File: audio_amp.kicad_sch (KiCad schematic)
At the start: 9 parts, among them Q1201 BSS138, U1201 LM380N

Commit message: Update pcb database to version 6
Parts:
- C1201, C1206: symbol Custom:C_US_0805_0.1UF_X7R_10%_50V_HS -> custom:C_US_0805_0.1UF_X7R_10%_50V_HS
- C1202, C1205: symbol Custom:CP_US -> custom:CP_US; PartNumber 800270-477 -> 80000X-XXX
- C1203, C1204: symbol Custom:C_US -> custom:C_US; PartNumber 800003-475 -> 800063-XXX
- Q1201: symbol Custom:BSS138 -> custom:BSS138
- R1201: symbol Custom:R_US_0805_1%_HS -> custom:R_US_0805_1%_HS; PartNumber 800235-027 -> 800235-XXX
- U1201: symbol Custom:LM380N -> custom:LM380N
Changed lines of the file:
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@@
     (effects (font (size 1.27 1.27)) (justify right))
   )
-  (symbol (lib_id "Custom:C_US") (at 67.31 90.17 270) (unit 1)
+  (symbol (lib_id "custom:C_US") (at 67.31 90.17 270) (unit 1)
     (in_bom yes) (on_board yes)
     (property "Reference" "C1204" (id 0) (at 67.31 83.3882 90))
@@
       (effects (font (size 1.524 1.524)))
     )
-    (property "PartNumber" "800003-475" (id 4) (at 81.28 90.17 0)
-      (effects (font (size 1.524 1.524)) hide)
-    )
-    (pin "1")
-    (pin "2")
-  )
-  (symbol (lib_id "Custom:LM380N") (at 129.54 95.25 0) (unit 1)
+    (property "PartNumber" "800063-XXX" (id 4) (at 81.28 90.17 0)
+      (effects (font (size 1.524 1.524)) hide)
+    )
+    (pin "1")
+    (pin "2")
+  )
+  (symbol (lib_id "custom:LM380N") (at 129.54 95.25 0) (unit 1)
     (in_bom yes) (on_board yes)
     (property "Reference" "U1201" (id 0) (at 139.7 88.9 0)
@@
     (pin "9")
   )
-  (symbol (lib_id "Custom:GND_US") (at 121.92 123.19 0) (unit 1)
+  (symbol (lib_id "custom:GND_US") (at 121.92 123.19 0) (unit 1)
     (in_bom yes) (on_board yes)
     (property "Reference" "#PWR01203" (id 0) (at 121.412 126.492 0)
@@
     (pin "1")
   )
-  (symbol (lib_id "Custom:C_US") (at 146.05 78.74 90) (unit 1)
+  (symbol (lib_id "custom:C_US") (at 146.05 78.74 90) (unit 1)
     (in_bom yes) (on_board yes)
     (property "Reference" "C1203" (id 0) (at 146.05 85.5218 90))
@@
       (effects (font (size 1.524 1.524)))
     )
-    (property "PartNumber" "800003-475" (id 4) (at 132.08 78.74 0)
-      (effects (font (size 1.524 1.524)) hide)
-    )
-    (pin "1")
-    (pin "2")
-  )
-  (symbol (lib_id "Custom:GND_US") (at 157.48 85.09 0) (unit 1)
+    (property "PartNumber" "800063-XXX" (id 4) (at 132.08 78.74 0)
+      (effects (font (size 1.524 1.524)) hide)
+    )
+    (pin "1")
+    (pin "2")
+  )
+  (symbol (lib_id "custom:GND_US") (at 157.48 85.09 0) (unit 1)
     (in_bom yes) (on_board yes)
     (property "Reference" "#PWR01201" (id 0) (at 156.972 88.392 0)
@@
     (pin "1")
   )
-  (symbol (lib_id "Custom:R_US_0805_1%_HS") (at 151.13 104.14 0) (unit 1)
+  (symbol (lib_id "custom:R_US_0805_1%_HS") (at 151.13 104.14 0) (unit 1)
     (in_bom yes) (on_board yes)
     (property "Reference" "R1201" (id 0) (at 152.654 102.9716 0)
@@
       (effects (font (size 1.524 1.524)))
     )
-    (property "PartNumber" "800235-027" (id 4) (at 155.702 101.6 90)
-      (effects (font (size 1.524 1.524)) hide)
-    )
-    (pin "1")
-    (pin "2")
-  )
-  (symbol (lib_id "Custom:C_US_0805_0.1UF_X7R_10%_50V_HS") (at 151.13 118.11 0) (unit 1)
+    (property "PartNumber" "800235-XXX" (id 4) (at 155.702 101.6 90)
+      (effects (font (size 1.524 1.524)) hide)
+    )
+    (pin "1")
+    (pin "2")
+  )
+  (symbol (lib_id "custom:C_US_0805_0.1UF_X7R_10%_50V_HS") (at 151.13 118.11 0) (unit 1)
     (in_bom yes) (on_board yes)
     (property "Reference" "C1206" (id 0) (at 154.432 116.9416 0)
@@
     (pin "2")
   )
-  (symbol (lib_id "Custom:GND_US") (at 151.13 123.19 0) (unit 1)
+  (symbol (lib_id "custom:GND_US") (at 151.13 123.19 0) (unit 1)
     (in_bom yes) (on_board yes)
     (property "Reference" "#PWR01204" (id 0) (at 150.622 126.492 0)
@@
     (pin "1")
   )
-  (symbol (lib_id "Custom:CP_US") (at 170.18 95.25 90) (unit 1)
+  (symbol (lib_id "custom:CP_US") (at 170.18 95.25 90) (unit 1)
     (in_bom yes) (on_board yes)
     (property "Reference" "C1205" (id 0) (at 170.18 88.4682 90))
@@
       (effects (font (size 1.524 1.524)))
     )
-    (property "PartNumber" "800270-477" (id 4) (at 165.1 91.44 0)
-      (effects (font (size 1.524 1.524)) hide)
-    )
-    (pin "1")
-    (pin "2")
-  )
-  (symbol (lib_id "Custom:CP_US") (at 140.97 69.85 90) (unit 1)
+    (property "PartNumber" "80000X-XXX" (id 4) (at 165.1 91.44 0)
+      (effects (font (size 1.524 1.524)) hide)
+    )
+    (pin "1")
+    (pin "2")
+  )
+  (symbol (lib_id "custom:CP_US") (at 140.97 69.85 90) (unit 1)
     (in_bom yes) (on_board yes)
     (property "Reference" "C1202" (id 0) (at 140.97 63.0682 90))
@@
       (effects (font (size 1.524 1.524)))
     )
-    (property "PartNumber" "800270-477" (id 4) (at 135.89 66.04 0)
-      (effects (font (size 1.524 1.524)) hide)
-    )
-    (pin "1")
-    (pin "2")
-  )
-  (symbol (lib_id "Custom:C_US_0805_0.1UF_X7R_10%_50V_HS") (at 140.97 58.42 90) (unit 1)
+    (property "PartNumber" "80000X-XXX" (id 4) (at 135.89 66.04 0)
+      (effects (font (size 1.524 1.524)) hide)
+    )
+    (pin "1")
+    (pin "2")
+  )
+  (symbol (lib_id "custom:C_US_0805_0.1UF_X7R_10%_50V_HS") (at 140.97 58.42 90) (unit 1)
     (in_bom yes) (on_board yes)
     (property "Reference" "C1201" (id 0) (at 140.97 51.6382 90))
@@
     (pin "2")
   )
-  (symbol (lib_id "Custom:BSS138") (at 53.34 111.76 0) (unit 1)
+  (symbol (lib_id "custom:BSS138") (at 53.34 111.76 0) (unit 1)
     (in_bom yes) (on_board yes)
     (property "Reference" "Q1201" (id 0) (at 58.7756 110.7948 0)
@@
     (pin "3")
   )
-  (symbol (lib_id "Custom:GND_US") (at 55.88 121.92 0) (unit 1)
+  (symbol (lib_id "custom:GND_US") (at 55.88 121.92 0) (unit 1)
     (in_bom yes) (on_board yes)
     (property "Reference" "#PWR01202" (id 0) (at 55.372 125.222 0)

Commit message: Fix BOM part number errors and out of sync footprints which happened during conversion from Kicad 5 to 6
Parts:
- C1202, C1205: PartNumber 80000X-XXX -> 800277-477
- C1203, C1204: PartNumber 800063-XXX -> 800003-475
- R1201: PartNumber 800235-XXX -> 800235-027
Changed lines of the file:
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@@
       (effects (font (size 1.524 1.524)))
     )
-    (property "PartNumber" "800063-XXX" (id 4) (at 81.28 90.17 0)
+    (property "PartNumber" "800003-475" (id 4) (at 81.28 90.17 0)
       (effects (font (size 1.524 1.524)) hide)
     )
@@
       (effects (font (size 1.524 1.524)))
     )
-    (property "PartNumber" "800063-XXX" (id 4) (at 132.08 78.74 0)
+    (property "PartNumber" "800003-475" (id 4) (at 132.08 78.74 0)
       (effects (font (size 1.524 1.524)) hide)
     )
@@
       (effects (font (size 1.524 1.524)))
     )
-    (property "PartNumber" "800235-XXX" (id 4) (at 155.702 101.6 90)
+    (property "PartNumber" "800235-027" (id 4) (at 155.702 101.6 90)
       (effects (font (size 1.524 1.524)) hide)
     )
@@
       (effects (font (size 1.524 1.524)))
     )
-    (property "PartNumber" "80000X-XXX" (id 4) (at 165.1 91.44 0)
+    (property "PartNumber" "800277-477" (id 4) (at 165.1 91.44 0)
       (effects (font (size 1.524 1.524)) hide)
     )
@@
       (effects (font (size 1.524 1.524)))
     )
-    (property "PartNumber" "80000X-XXX" (id 4) (at 135.89 66.04 0)
+    (property "PartNumber" "800277-477" (id 4) (at 135.89 66.04 0)
       (effects (font (size 1.524 1.524)) hide)
     )

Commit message: Fix incorrect part number for 470uf capacitor
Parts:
- C1202, C1205: PartNumber 800277-477 -> 800270-477
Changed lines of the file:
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@@
       (effects (font (size 1.524 1.524)))
     )
-    (property "PartNumber" "800277-477" (id 4) (at 165.1 91.44 0)
+    (property "PartNumber" "800270-477" (id 4) (at 165.1 91.44 0)
       (effects (font (size 1.524 1.524)) hide)
     )
@@
       (effects (font (size 1.524 1.524)))
     )
-    (property "PartNumber" "800277-477" (id 4) (at 135.89 66.04 0)
+    (property "PartNumber" "800270-477" (id 4) (at 135.89 66.04 0)
       (effects (font (size 1.524 1.524)) hide)
     )

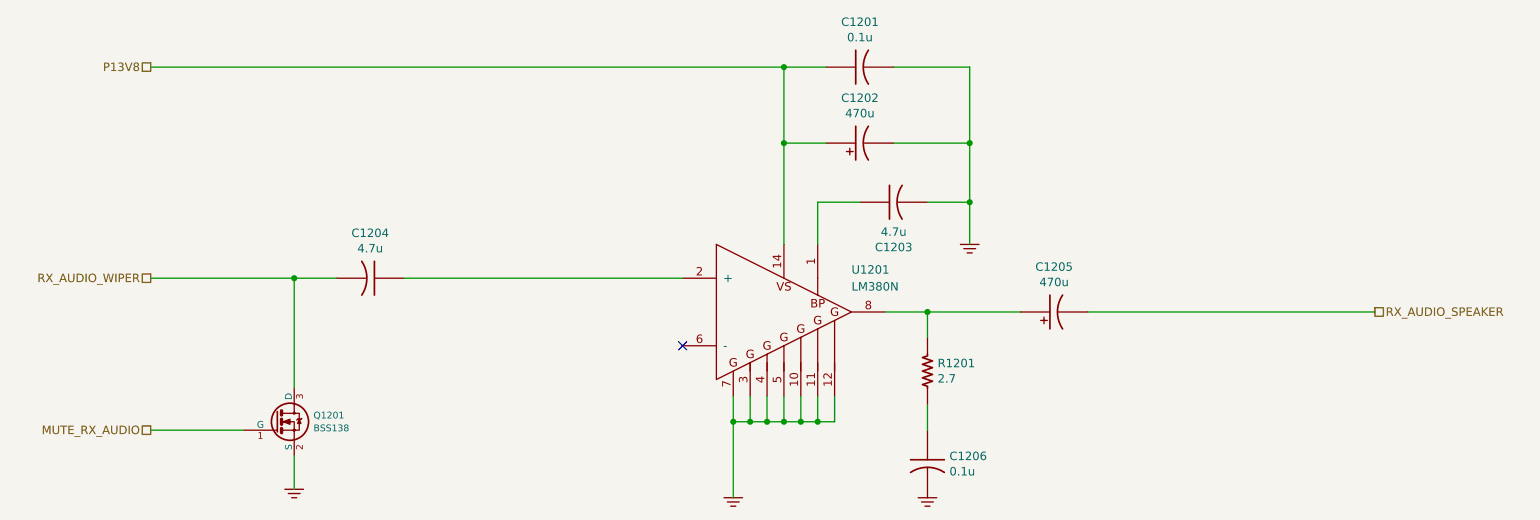
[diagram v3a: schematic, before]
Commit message: trx_mobo_concept_2_B. Change design to use a dedicated 8V supply for the 2SC3357 parts. Add S-Meter connector. Change mic connector to 3 pins and add 8V sopower supply to pin 3.
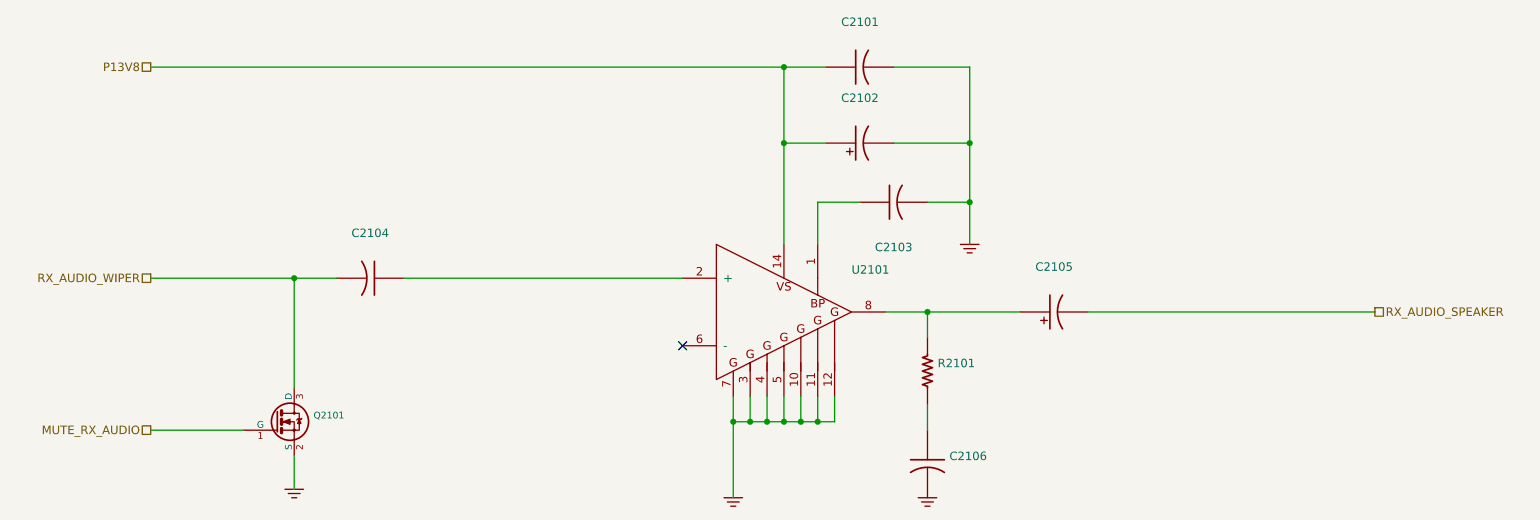
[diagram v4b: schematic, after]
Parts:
- C2101: renamed from C1201; value 0.1u -> (none); footprint Capacitor_SMD:C_0805_2012Metric_Pad1.15x1.40mm_HandSolder -> (none)
- C2102: renamed from C1202; value 470u -> (none); footprint Capacitor_SMD:CP_Elec_10x10 -> (none)
- C2103: renamed from C1203; value 4.7u -> (none); footprint Capacitor_SMD:C_0805_2012Metric_Pad1.15x1.40mm_HandSolder -> (none)
- C2104: renamed from C1204; value 4.7u -> (none); footprint Capacitor_SMD:C_0805_2012Metric_Pad1.15x1.40mm_HandSolder -> (none)
- C2105: renamed from C1205; value 470u -> (none); footprint Capacitor_SMD:CP_Elec_10x10 -> (none)
- C2106: renamed from C1206; value 0.1u -> (none); footprint Capacitor_SMD:C_0805_2012Metric_Pad1.15x1.40mm_HandSolder -> (none)
- Q2101: renamed from Q1201; value BSS138 -> (none); footprint mods:SOT23-3-SAR -> (none)
- R2101: renamed from R1201; value 2.7 -> (none); footprint Resistor_SMD:R_0805_2012Metric_Pad1.15x1.40mm_HandSolder -> (none)
- U2101: renamed from U1201; value LM380N -> (none); footprint Package_DIP:DIP-14_W7.62mm_Socket_LongPads -> (none)
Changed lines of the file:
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@@
   (title_block
     (title "Speaker Audio Amplifier")
-    (rev "X1")
+    (rev "B")
     (company "WA6ZFT")
   )
@@
   (symbol (lib_id "custom:C_US") (at 67.31 90.17 270) (unit 1)
     (in_bom yes) (on_board yes)
-    (property "Reference" "C1204" (id 0) (at 67.31 83.3882 90))
-    (property "Value" "4.7u" (id 1) (at 67.31 85.6996 90))
-    (property "Footprint" "Capacitor_SMD:C_0805_2012Metric_Pad1.15x1.40mm_HandSolder" (id 2) (at 78.74 92.71 0)
+    (property "Reference" "C2104" (id 0) (at 67.31 83.3882 90))
+    (property "Value" "" (id 1) (at 67.31 85.6996 90))
+    (property "Footprint" "" (id 2) (at 78.74 92.71 0)
       (effects (font (size 1.524 1.524)) hide)
     )
@@
   (symbol (lib_id "custom:LM380N") (at 129.54 95.25 0) (unit 1)
     (in_bom yes) (on_board yes)
-    (property "Reference" "U1201" (id 0) (at 139.7 88.9 0)
-      (effects (font (size 1.27 1.27)) (justify left))
-    )
-    (property "Value" "LM380N" (id 1) (at 139.7 91.44 0)
-      (effects (font (size 1.27 1.27)) (justify left))
-    )
-    (property "Footprint" "Package_DIP:DIP-14_W7.62mm_Socket_LongPads" (id 2) (at 129.54 110.49 0)
+    (property "Reference" "U2101" (id 0) (at 139.7 88.9 0)
+      (effects (font (size 1.27 1.27)) (justify left))
+    )
+    (property "Value" "" (id 1) (at 139.7 91.44 0)
+      (effects (font (size 1.27 1.27)) (justify left))
+    )
+    (property "Footprint" "" (id 2) (at 129.54 110.49 0)
       (effects (font (size 1.27 1.27)) hide)
     )
@@
   (symbol (lib_id "custom:GND_US") (at 121.92 123.19 0) (unit 1)
     (in_bom yes) (on_board yes)
-    (property "Reference" "#PWR01203" (id 0) (at 121.412 126.492 0)
+    (property "Reference" "#PWR02103" (id 0) (at 121.412 126.492 0)
       (effects (font (size 0.762 0.762)) hide)
     )
@@
   (symbol (lib_id "custom:C_US") (at 146.05 78.74 90) (unit 1)
     (in_bom yes) (on_board yes)
-    (property "Reference" "C1203" (id 0) (at 146.05 85.5218 90))
-    (property "Value" "4.7u" (id 1) (at 146.05 83.2104 90))
-    (property "Footprint" "Capacitor_SMD:C_0805_2012Metric_Pad1.15x1.40mm_HandSolder" (id 2) (at 134.62 76.2 0)
+    (property "Reference" "C2103" (id 0) (at 146.05 85.5218 90))
+    (property "Value" "" (id 1) (at 146.05 83.2104 90))
+    (property "Footprint" "" (id 2) (at 134.62 76.2 0)
       (effects (font (size 1.524 1.524)) hide)
     )
@@
   (symbol (lib_id "custom:GND_US") (at 157.48 85.09 0) (unit 1)
     (in_bom yes) (on_board yes)
-    (property "Reference" "#PWR01201" (id 0) (at 156.972 88.392 0)
+    (property "Reference" "#PWR02101" (id 0) (at 156.972 88.392 0)
       (effects (font (size 0.762 0.762)) hide)
     )
@@
   (symbol (lib_id "custom:R_US_0805_1%_HS") (at 151.13 104.14 0) (unit 1)
     (in_bom yes) (on_board yes)
-    (property "Reference" "R1201" (id 0) (at 152.654 102.9716 0)
-      (effects (font (size 1.27 1.27)) (justify left))
-    )
-    (property "Value" "2.7" (id 1) (at 152.654 105.283 0)
-      (effects (font (size 1.27 1.27)) (justify left))
-    )
-    (property "Footprint" "Resistor_SMD:R_0805_2012Metric_Pad1.15x1.40mm_HandSolder" (id 2) (at 151.13 104.14 0)
+    (property "Reference" "R2101" (id 0) (at 152.654 102.9716 0)
+      (effects (font (size 1.27 1.27)) (justify left))
+    )
+    (property "Value" "" (id 1) (at 152.654 105.283 0)
+      (effects (font (size 1.27 1.27)) (justify left))
+    )
+    (property "Footprint" "" (id 2) (at 151.13 104.14 0)
       (effects (font (size 1.524 1.524)) hide)
     )
@@
   (symbol (lib_id "custom:C_US_0805_0.1UF_X7R_10%_50V_HS") (at 151.13 118.11 0) (unit 1)
     (in_bom yes) (on_board yes)
-    (property "Reference" "C1206" (id 0) (at 154.432 116.9416 0)
-      (effects (font (size 1.27 1.27)) (justify left))
-    )
-    (property "Value" "0.1u" (id 1) (at 154.432 119.253 0)
-      (effects (font (size 1.27 1.27)) (justify left))
-    )
-    (property "Footprint" "Capacitor_SMD:C_0805_2012Metric_Pad1.15x1.40mm_HandSolder" (id 2) (at 153.67 106.68 0)
+    (property "Reference" "C2106" (id 0) (at 154.432 116.9416 0)
+      (effects (font (size 1.27 1.27)) (justify left))
+    )
+    (property "Value" "" (id 1) (at 154.432 119.253 0)
+      (effects (font (size 1.27 1.27)) (justify left))
+    )
+    (property "Footprint" "" (id 2) (at 153.67 106.68 0)
       (effects (font (size 1.524 1.524)) hide)
     )
@@
   (symbol (lib_id "custom:GND_US") (at 151.13 123.19 0) (unit 1)
     (in_bom yes) (on_board yes)
-    (property "Reference" "#PWR01204" (id 0) (at 150.622 126.492 0)
+    (property "Reference" "#PWR02104" (id 0) (at 150.622 126.492 0)
       (effects (font (size 0.762 0.762)) hide)
     )
@@
   (symbol (lib_id "custom:CP_US") (at 170.18 95.25 90) (unit 1)
     (in_bom yes) (on_board yes)
-    (property "Reference" "C1205" (id 0) (at 170.18 88.4682 90))
-    (property "Value" "470u" (id 1) (at 170.18 90.7796 90))
-    (property "Footprint" "Capacitor_SMD:CP_Elec_10x10" (id 2) (at 170.18 90.6018 90)
+    (property "Reference" "C2105" (id 0) (at 170.18 88.4682 90))
+    (property "Value" "" (id 1) (at 170.18 90.7796 90))
+    (property "Footprint" "" (id 2) (at 170.18 90.6018 90)
       (effects (font (size 1.524 1.524)) hide)
     )
@@
   (symbol (lib_id "custom:CP_US") (at 140.97 69.85 90) (unit 1)
     (in_bom yes) (on_board yes)
-    (property "Reference" "C1202" (id 0) (at 140.97 63.0682 90))
-    (property "Value" "470u" (id 1) (at 140.97 65.3796 90))
-    (property "Footprint" "Capacitor_SMD:CP_Elec_10x10" (id 2) (at 140.97 65.2018 90)
+    (property "Reference" "C2102" (id 0) (at 140.97 63.0682 90))
+    (property "Value" "" (id 1) (at 140.97 65.3796 90))
+    (property "Footprint" "" (id 2) (at 140.97 65.2018 90)
       (effects (font (size 1.524 1.524)) hide)
     )
@@
   (symbol (lib_id "custom:C_US_0805_0.1UF_X7R_10%_50V_HS") (at 140.97 58.42 90) (unit 1)
     (in_bom yes) (on_board yes)
-    (property "Reference" "C1201" (id 0) (at 140.97 51.6382 90))
-    (property "Value" "0.1u" (id 1) (at 140.97 53.9496 90))
-    (property "Footprint" "Capacitor_SMD:C_0805_2012Metric_Pad1.15x1.40mm_HandSolder" (id 2) (at 129.54 55.88 0)
+    (property "Reference" "C2101" (id 0) (at 140.97 51.6382 90))
+    (property "Value" "" (id 1) (at 140.97 53.9496 90))
+    (property "Footprint" "" (id 2) (at 129.54 55.88 0)
       (effects (font (size 1.524 1.524)) hide)
     )
@@
   (symbol (lib_id "custom:BSS138") (at 53.34 111.76 0) (unit 1)
     (in_bom yes) (on_board yes)
-    (property "Reference" "Q1201" (id 0) (at 58.7756 110.7948 0)
+    (property "Reference" "Q2101" (id 0) (at 58.7756 110.7948 0)
       (effects (font (size 1.016 1.016)) (justify left))
     )
-    (property "Value" "BSS138" (id 1) (at 58.7756 112.7252 0)
+    (property "Value" "" (id 1) (at 58.7756 112.7252 0)
       (effects (font (size 1.016 1.016)) (justify left))
     )
-    (property "Footprint" "mods:SOT23-3-SAR" (id 2) (at 50.038 109.1692 0)
+    (property "Footprint" "" (id 2) (at 50.038 109.1692 0)
       (effects (font (size 0.7366 0.7366)) hide)
     )
@@
   (symbol (lib_id "custom:GND_US") (at 55.88 121.92 0) (unit 1)
     (in_bom yes) (on_board yes)
-    (property "Reference" "#PWR01202" (id 0) (at 55.372 125.222 0)
-      (effects (font (size 0.762 0.762)) hide)
-    )
+    (property "Reference" "#PWR02102" (id 0) (at 55.372 125.222 0)
+      (effects (font (size 0.762 0.762)) hide)
+    )
